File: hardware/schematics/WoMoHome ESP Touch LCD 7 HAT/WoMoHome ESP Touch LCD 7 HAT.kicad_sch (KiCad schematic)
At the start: 8 parts, among them J1 I2C (2), J2 I2C (1), J3 GasWaage, J4 Conn_01x02, SW1 SW_Push, U1 DPT_Walter, U2 BNO055, U3 ISL3298xxRT

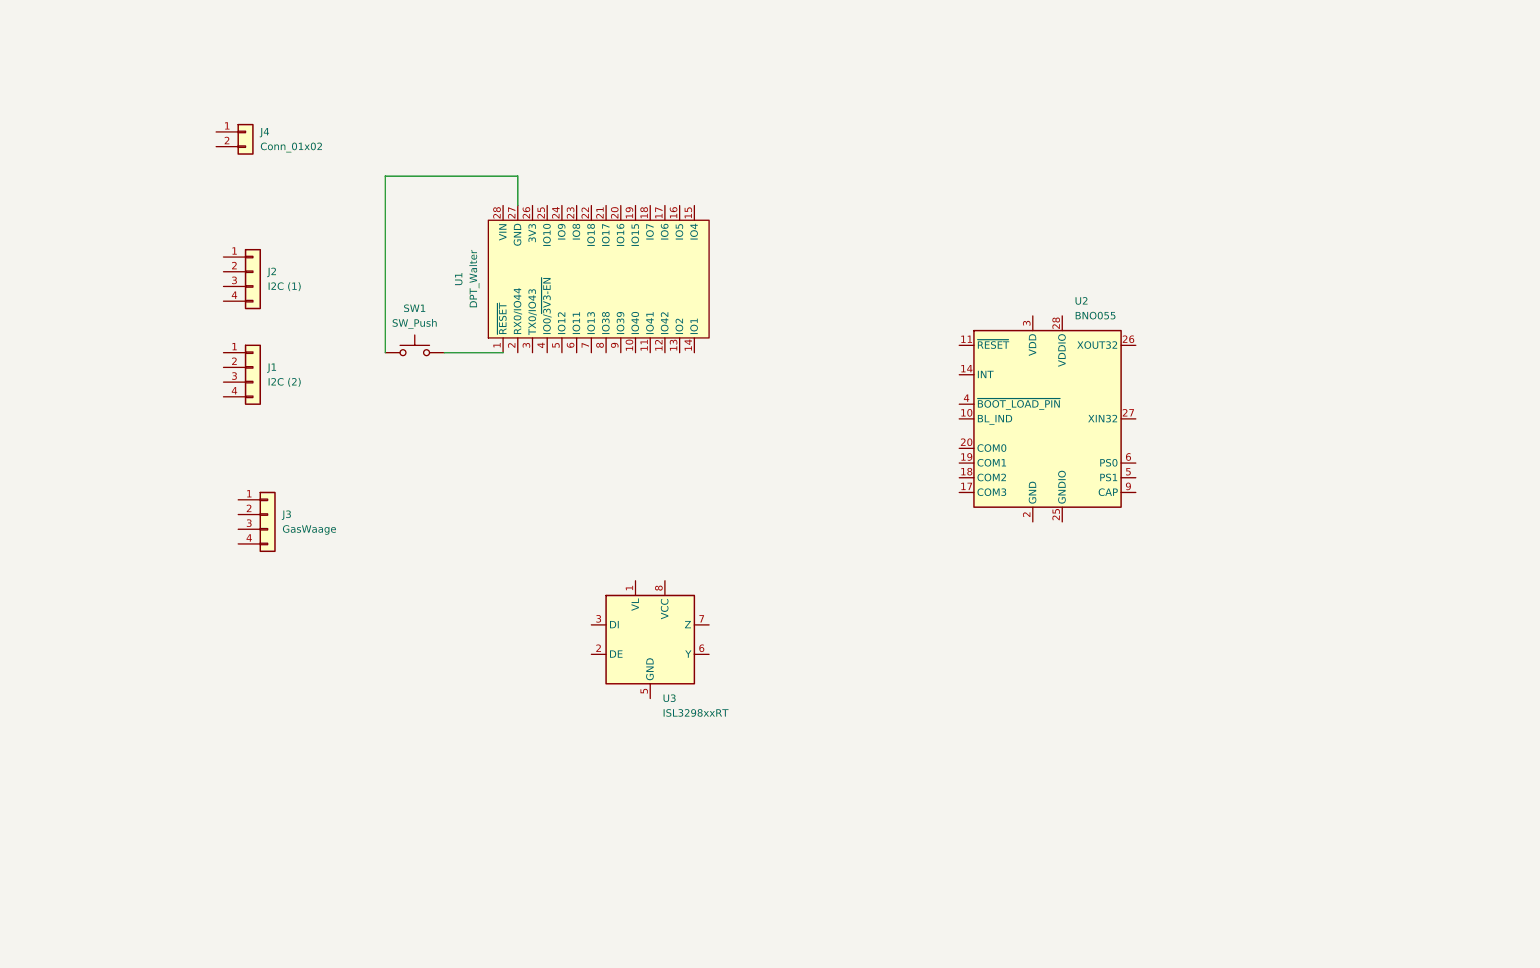
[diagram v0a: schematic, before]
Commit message: refactor: Alle Firmware-Projekte und ungetrackte Dateien sichern
- firmware-modem/ (Sensorboard via USB-Modem) hinzugefügt
- firmware-sensor/ (Sensorboard standalone, künftig aktiv) hinzugefügt
- Alle lokalen Änderungen an firmware/, firmware-walter/, docs/, hardware/ gesichert
- Basis-Commit vor großer Umstrukturierung
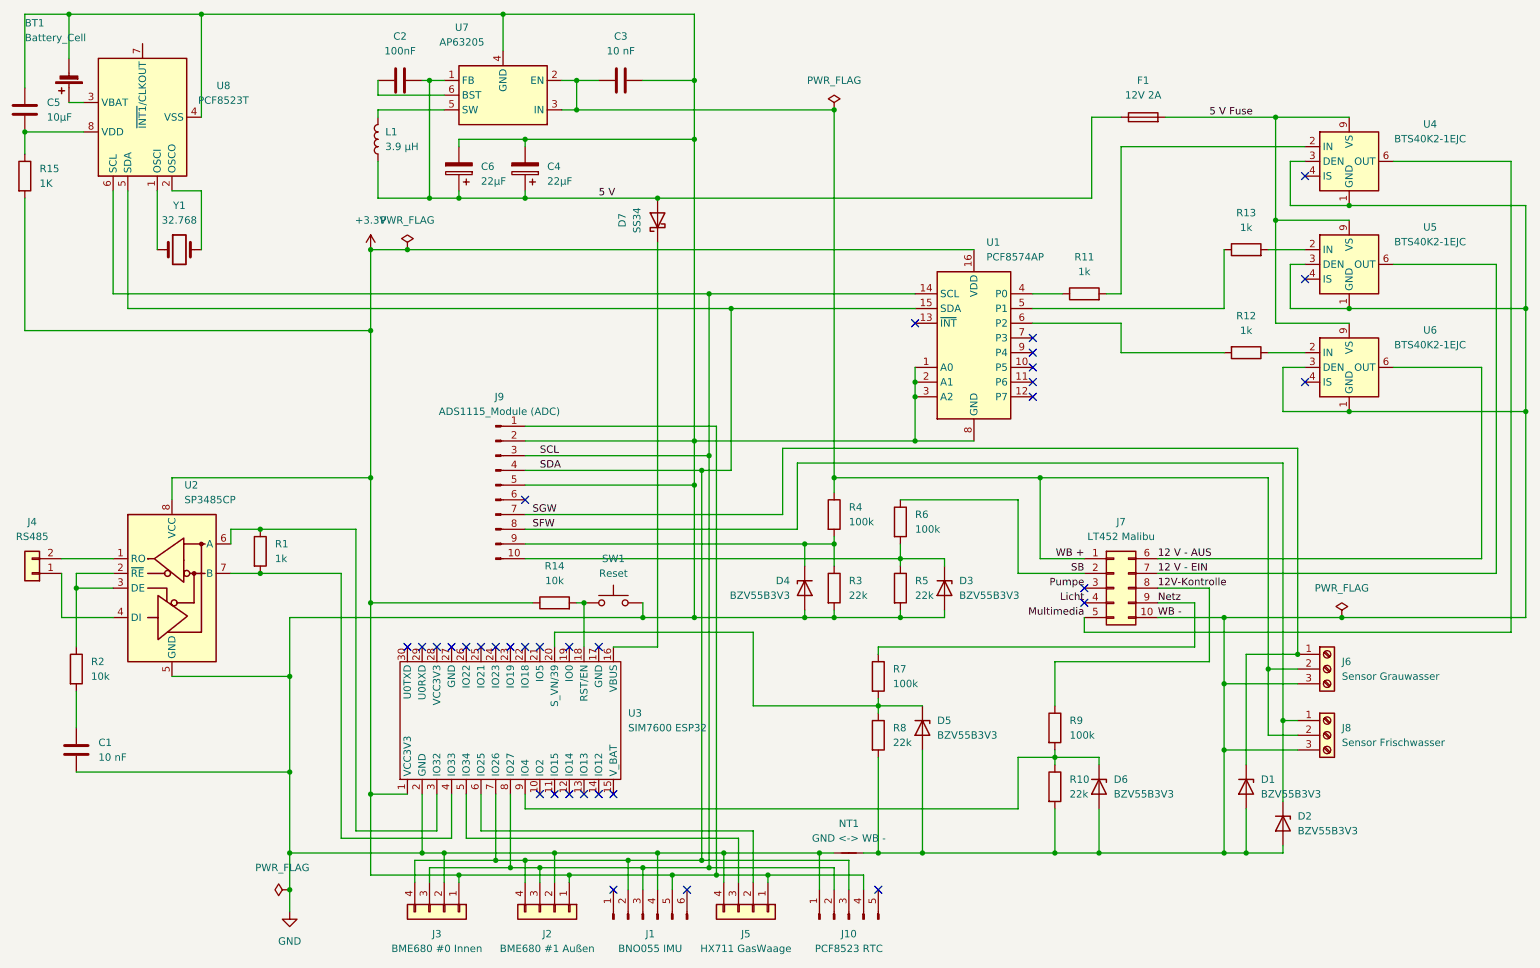
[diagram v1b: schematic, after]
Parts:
- removed J1: I2C (2), symbol Connector_Generic:Conn_01x04
- removed U1: DPT_Walter, symbol WoMoHome:DPT_Walter
- removed U2: BNO055, Package_LGA:LGA-28_5.2x3.8mm_P0.5mm, symbol Sensor_Motion:BNO055
- removed U3: ISL3298xxRT, Package_DFN_QFN:TDFN-8-1EP_3x2mm_P0.5mm_EP1.80x1.65mm, symbol Interface_UART:ISL3298xxRT
- added BT1: Battery_Cell, symbol Device:Battery_Cell
- added C1, C3: 10 nF, Capacitor_SMD:C_0805_2012Metric_Pad1.18x1.45mm_HandSolder, symbol Device:C
- added C2: 100nF, Capacitor_SMD:C_0805_2012Metric_Pad1.18x1.45mm_HandSolder, symbol Device:C
- added C4, C6: 22µF, Capacitor_SMD:C_1206_3216Metric_Pad1.33x1.80mm_HandSolder, symbol Device:C_Polarized
- added C5: 10µF, symbol Device:C
- added D1, D2, D3, D4, D5, D6: BZV55B3V3, Diode_SMD:D_MiniMELF, symbol Diode:BZV55B3V3
- added D7: SS34, Diode_SMD:D_SMA, symbol Diode:SS34
- added F1: 12V 2A, Fuse:Fuse_1210_3225Metric_Pad1.42x2.65mm_HandSolder, symbol Device:Fuse
- added J1: BNO055 IMU, Connector_PinHeader_2.54mm:PinHeader_1x06_P2.54mm_Vertical, symbol Connector:Conn_01x06_Pin
- added J10: PCF8523 RTC, Connector_PinHeader_2.54mm:PinHeader_1x05_P2.54mm_Vertical, symbol Connector:Conn_01x05_Pin
- added J3: BME680 #0 Innen, Connector_JST:JST_XH_B4B-XH-A_1x04_P2.50mm_Vertical, symbol Connector_Generic:Conn_01x04
- added J6: Sensor Grauwasser, TerminalBlock_Phoenix:TerminalBlock_Phoenix_PT-1,5-3-5.0-H_1x03_P5.00mm_Horizontal, symbol Connector:Screw_Terminal_01x03
- added J7: LT452 Malibu, Connector_Molex:Molex_Micro-Fit_3.0_43045-1012_2x05_P3.00mm_Vertical, symbol Connector_Generic:Conn_02x05_Top_Bottom
- added J8: Sensor Frischwasser, TerminalBlock_Phoenix:TerminalBlock_Phoenix_PT-1,5-3-5.0-H_1x03_P5.00mm_Horizontal, symbol Connector:Screw_Terminal_01x03
- added J9: ADS1115_Module (ADC), Connector_PinHeader_2.54mm:PinHeader_1x10_P2.54mm_Vertical, symbol Connector:Conn_01x10_Pin
- added L1: 3.9 µH, Inductor_SMD_Wurth:L_Wurth_WE-LQSH-4020, symbol Device:L
- added NT1: GND <-> WB -, symbol Device:NetTie_2
- added R1, R11, R12, R13: 1k, Resistor_SMD:R_0805_2012Metric_Pad1.20x1.40mm_HandSolder, symbol Device:R
- added R10, R3, R5, R8: 22k, Resistor_SMD:R_0805_2012Metric_Pad1.20x1.40mm_HandSolder, symbol Device:R
- added R14, R2: 10k, Resistor_SMD:R_0805_2012Metric_Pad1.20x1.40mm_HandSolder, symbol Device:R
- added R15: 1K, symbol Device:R
- added R4, R6, R7, R9: 100k, Resistor_SMD:R_0805_2012Metric_Pad1.20x1.40mm_HandSolder, symbol Device:R
- added U1: PCF8574AP, Package_DIP:DIP-16_W7.62mm, symbol Interface_Expansion:PCF8574AP
- added U2: SP3485CP, Package_DIP:DIP-8_W7.62mm, symbol Interface_UART:SP3485CP
- added U3: SIM7600 ESP32, WoMoHome:SIM7600X-ESP32, symbol WoMoHome:SIM7600X-ESP32
- added U4, U5, U6: BTS40K2-1EJC, Package_SO:Infineon_PG-DSO-8-43, symbol Power_Management:BTS40K2-1EJC
- added U7: AP63205, Package_TO_SOT_SMD:TSOT-23-6, symbol Regulator_Switching:AP63203WU
- added U8: PCF8523T, Package_SO:SOIC-8_3.9x4.9mm_P1.27mm, symbol Timer_RTC:PCF8523T
- added Y1: 32.768, symbol Device:Crystal
- J2: value I2C (1) -> BME680 #1 Außen; footprint (none) -> Connector_JST:JST_XH_B4B-XH-A_1x04_P2.50mm_Vertical
- J4: value Conn_01x02 -> RS485; footprint (none) -> Connector_JST:JST_XH_B2B-XH-A_1x02_P2.50mm_Vertical
- J5: renamed from J3; value GasWaage -> HX711 GasWaage; footprint (none) -> Connector_JST:JST_XH_B4B-XH-A_1x04_P2.50mm_Vertical
- SW1: value SW_Push -> Reset; footprint (none) -> Button_Switch_THT:SW_PUSH_6mm
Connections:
- net GND: now reaches SW1.2
- net GND: now also J2.2 (Pin_2), J5.4 (Pin_4), BT1.2 (-), C1.2, C3.2, C4.2, C5.1, C6.2, D3.2 (A), D4.2 (A), J1.4 (Pin_4), J10.1 (Pin_1), J3.2 (Pin_2), J9.2 (Pin_2), J9.5 (Pin_5), NT1.1, R3.2, R5.2, U1.1 (A0), U1.2 (A1), U1.3 (A2), U1.8 (GND), U2.5 (GND), U3.2 (GND), U7.4 (GND), U8.4 (VSS)
- net at SW1.1: now also R14.2, U3.18 (RST/EN)
- net at J4.1 (Pin_1): now also U2.4 (DI)
- net at J4.2 (Pin_2): now also U2.1 (RO)
- net +3.3V: now reaches J2.1 (Pin_1)
- net +3.3V: now also J5.1 (Pin_1), J1.5 (Pin_5), J10.4 (Pin_4), J3.1 (Pin_1), J9.1 (Pin_1), R14.1, R15.2, U1.16 (VDD), U2.8 (VCC), U3.1 (VCC3V3)
- net SCL: now reaches J2.3 (Pin_3)
- net SCL: now also J1.3 (Pin_3), J10.2 (Pin_2), J3.3 (Pin_3), J9.3 (Pin_3), U1.14 (SCL), U3.8 (IO27), U8.6 (SCL)
- net SDA: now reaches J2.4 (Pin_4)
- net SDA: now also J1.2 (Pin_2), J10.3 (Pin_3), J3.4 (Pin_4), J9.4 (Pin_4), U1.15 (SDA), U3.7 (IO26), U8.5 (SDA)
- net at J5.2 (Pin_2): now also U3.6 (IO25)
- net at J5.3 (Pin_3): now also U3.5 (IO34)
- new net: D5.1 (K), R7.2, R8.1, U3.20 (S_VN/39)
- new net: C1.1, R2.2
- new net: D4.1 (K), J9.9 (Pin_9), R3.1, R4.2
- new net: R12.1, U6.2 (IN)
- new net: R12.2, U1.6 (P2)
- new net: U8.1 (OSCI), Y1.1
- new net: U8.2 (OSCO), Y1.2
- new net: BT1.1 (+), U8.3 (VBAT)
- new net: C5.2, R15.1, U8.8 (VDD)
- new net: L1.2, U7.5 (SW)
- new net: C2.1, U7.6 (BST)
- new net: D3.1 (K), J9.10 (Pin_10), R5.1, R6.2
- new net: R11.1, U1.4 (P0)
- new net: R11.2, U4.2 (IN)
- new net: D7.1 (K), U3.16 (VBUS)
- new net: R1.1, U2.6 (A), U3.3 (IO32)
- new net: R1.2, U2.7 (B), U3.4 (IO33)
- new net: D6.1 (K), R10.1, R9.2, U3.9 (IO4)
- new net: R2.1, U2.2 (~{RE}), U2.3 (DE)
- new net: R13.1, U1.5 (P1)
- new net: R13.2, U5.2 (IN)
- new net 12 V - AUS: J7.6 (Pin_6), U6.6 (OUT), U6.7 (OUT), U6.8 (OUT)
- new net 12 V - EIN: J7.7 (Pin_7), U5.6 (OUT), U5.7 (OUT), U5.8 (OUT)
- new net 12V-Kontrolle: J7.8 (Pin_8), R9.1
- new net 5 V: C2.2, C4.1, C6.1, D7.2 (A), F1.1, L1.1, U7.1 (FB)
- new net 5 V Fuse: F1.2, U4.9 (VS), U5.9 (VS), U6.9 (VS)
- new net Licht: J7.4 (Pin_4)
- new net Multimedia: J7.5 (Pin_5), U4.6 (OUT), U4.7 (OUT), U4.8 (OUT)
- new net Netz: J7.9 (Pin_9), R7.1
- new net Pumpe: J7.3 (Pin_3)
- new net SB: J7.2 (Pin_2), R6.1
- new net SFW: D2.1 (K), J8.1 (Pin_1), J9.8 (Pin_8)
- new net SGW: D1.1 (K), J6.1 (Pin_1), J9.7 (Pin_7)
- new net WB +: C3.1, J6.2 (Pin_2), J7.1 (Pin_1), J8.2 (Pin_2), R4.1, U7.2 (EN), U7.3 (IN)
- new net WB -: D1.2 (A), D2.2 (A), D5.2 (A), D6.2 (A), J6.3 (Pin_3), J7.10 (Pin_10), J8.3 (Pin_3), NT1.2, R10.2, R8.2, U4.1 (GND), U4.3 (DEN), U5.1 (GND), U5.3 (DEN), U6.1 (GND), U6.3 (DEN)
- no-connect marks 0 -> 33
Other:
- title: (none) -> WoMoHome Control
- moved on the sheet: J2, J4, J5, SW1
